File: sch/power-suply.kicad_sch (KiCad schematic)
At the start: 38 parts, among them J5 12V_in, Q2 DMT6007LFG-7, U1 LMR51450SDRRR, U2 LM74700QDBVTQ1, U3 LMR51450SDRRR

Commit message: update licence to CERN-OHL-S
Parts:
- D2: DESCRIPTION ESD Suppressor Diode Polymer Bi-Dir 30V 2-Pin Case 0402(100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 -> (none)
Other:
- company: (none) -> NTNU, NINA
- title: (none) -> Audiograb

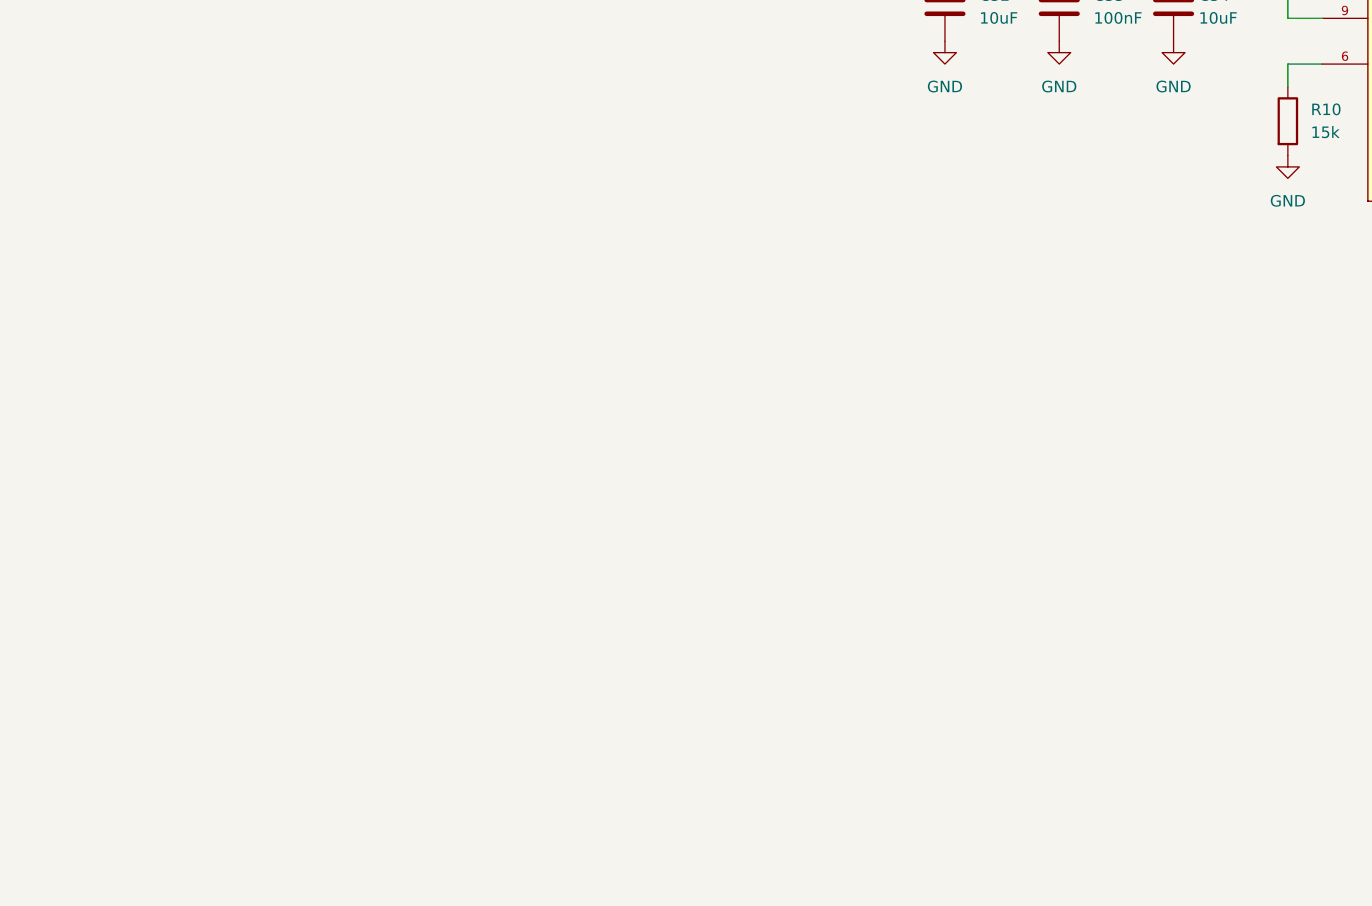
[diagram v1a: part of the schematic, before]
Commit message: Ryddet i schematic og satt inn 3D figurer
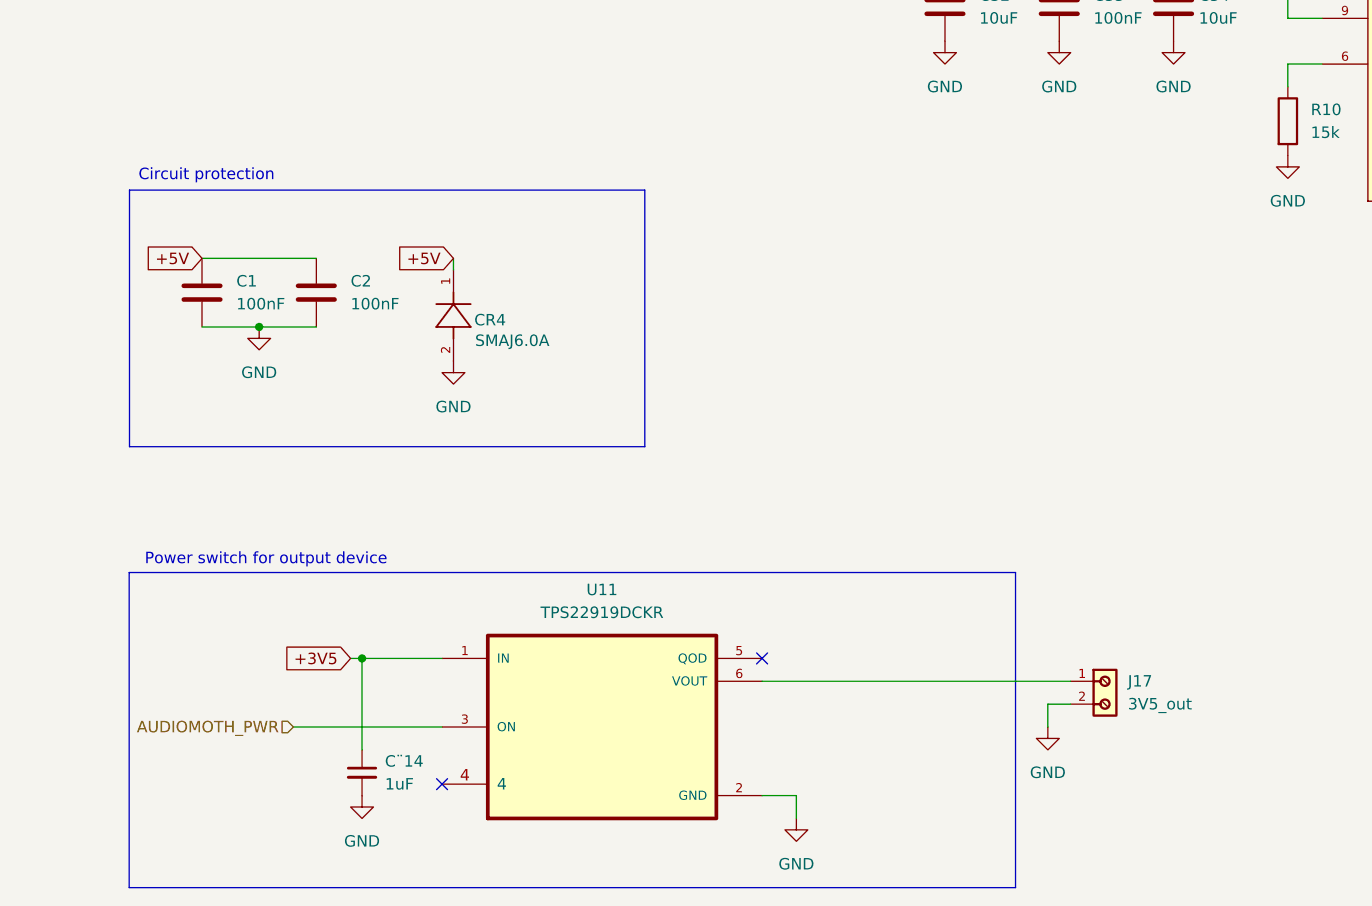
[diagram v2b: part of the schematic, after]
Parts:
- added C1, C2: 100nF, Capacitor_SMD:C_0603_1608Metric, symbol Device:C
- added CR4: SMAJ6.0A, SMAJ6.0A:DIOM4325X250N, symbol SMAJ6.0A:SMAJ6.0A
- added C¨14: 1uF, Capacitor_SMD:C_0603_1608Metric, symbol Device:C_Small
- added J17: 3V5_out, 691137710002:691137710002, symbol 691137710002:691137710002
- added U11: TPS22919DCKR, TPS22919DCKR:SOT65P210X110-6N, symbol TPS22919DCKR:TPS22919DCKR
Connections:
- net +3V5: now also C¨14.1, U11.1 (IN)
- net +5V: now also C1.1, C2.1, CR4.1
- net GND: now also C1.2, C2.2, CR4.2, C¨14.2, J17.2, U11.2 (GND)
- new net: J17.1, U11.6 (VOUT)
- new net AUDIOMOTH_PWR: U11.3 (ON)
- no-connect marks 2 -> 4
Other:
- note added: "Circuit protection"
- note added: "Power switch for output device"
